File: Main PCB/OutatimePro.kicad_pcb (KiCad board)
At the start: 2 copper layers, 25.7 x 27.7 mm, 47 parts, among them IC1 PAM8904JPR, J1 USB_B_Micro_PCB_Edge_receptac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, J2 FH35C-9S-0.3SHW, J3 OSO_SWD, Q1 ALS-PT19-315C/L177/TR8, SW1 EVPAWED40, U1 ATSAML22N18A-CFUT, U2 MIC5365-3.3YMT, U3 USBLC6-2P6, U4 MAX40200ANS, Y1 32.768kHz

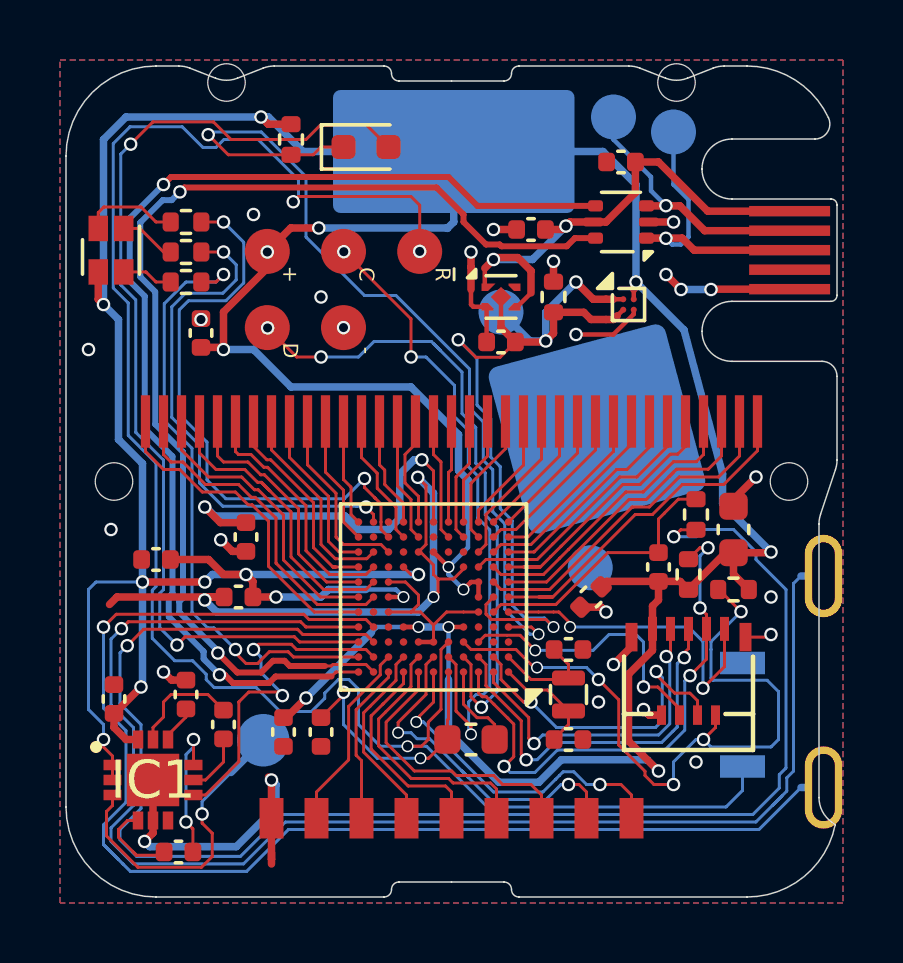
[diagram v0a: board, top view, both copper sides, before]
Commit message: move test pads to a good location
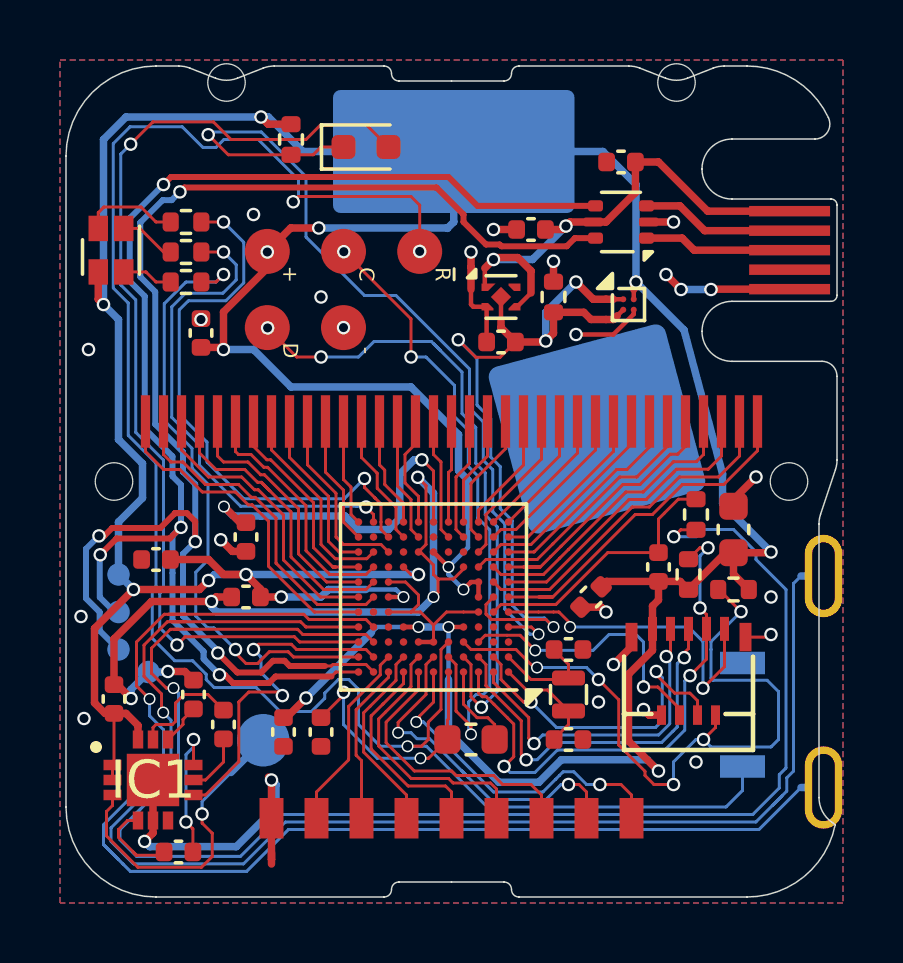
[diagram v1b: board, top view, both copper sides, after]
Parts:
- TP1, TP2, TP3, TP4: footprint OutatimePro:TestPoint_Pad_D1.5mm -> OutatimePro:TestPoint_Pad_D0.75mm
- moved TP1 25.3 mm to (14.8, 32.8)
- moved TP2 23.3 mm to (14.8, 31.5)
- moved TP3 15.5 mm to (14.8, 30.2)
- moved TP4 15.1 mm to (15.8, 33.5)
- moved C16 0.25 mm to (17.2, 34.2)
- moved C5 0.25 mm to (19.0, 31.0)
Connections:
- TP1 pad 1: Net-(J1-D+) -> /USB_P
- TP2 pad 1: Net-(J1-D-) -> /USB_N
- TP3 pad 1: +3.3V -> VCC
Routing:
- net /USB_P: track 38.1 -> 47.3 mm, vias 2 -> 4
- net /USB_N: track 38.0 -> 43.4 mm, vias 2 -> 4
- net VCC: track 151.5 -> 146.6 mm, vias 21 -> 19
- net Net-(J1-D+): track 9.59 -> 4.94 mm, vias 1 -> 0
- net GND: track 59.3 -> 63.2 mm, vias 29 -> 31
- net Net-(J1-D-): track 8.79 -> 5.11 mm, vias 1 -> 0
- net +3.3V: track 29.2 -> 27.3 mm
- net /VLCD: track 13.2 -> 11.9 mm
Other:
- board text added: "D+"
- board text added: "D-"
- board text added: "G"
- board text added: "V"

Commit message: move test pads more and change version format
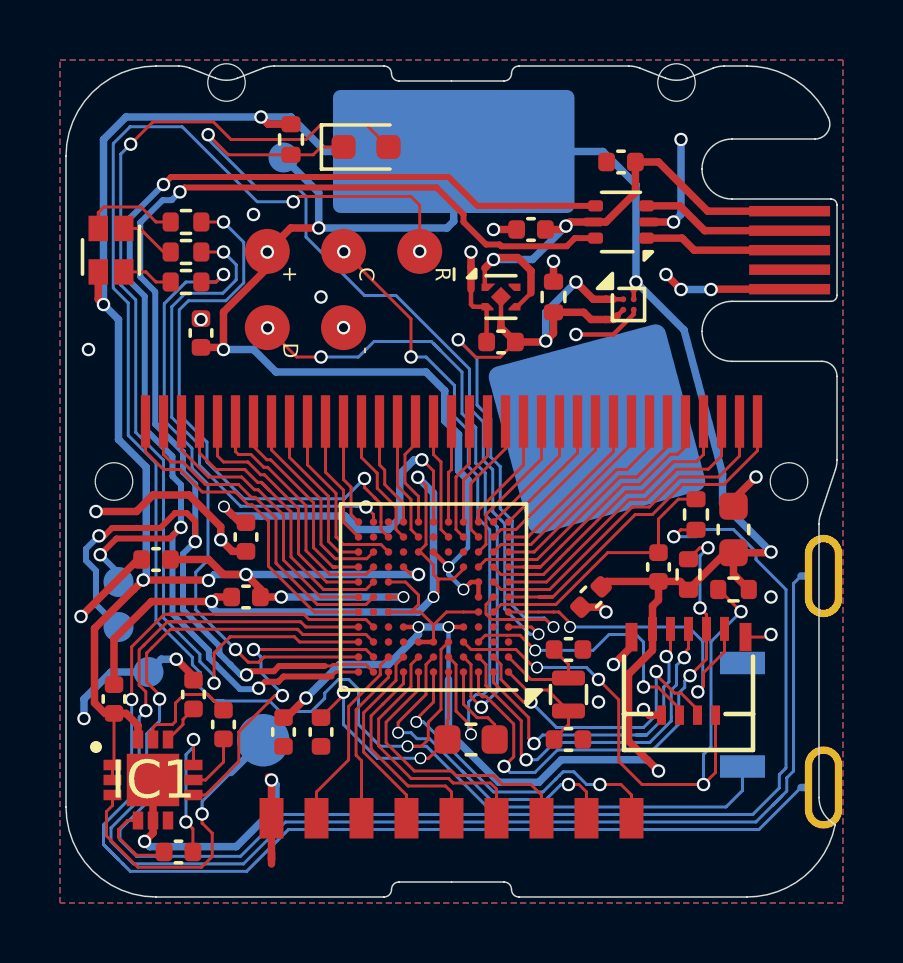
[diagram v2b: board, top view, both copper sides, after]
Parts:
- TP1, TP2, TP3, TP4: footprint OutatimePro:TestPoint_Pad_D0.75mm -> OutatimePro:TestPoint_Pad_D1.0mm
- moved TP3 14.9 mm to (20.2, 16.4)
- moved TP2 1.00 mm to (14.8, 30.5)
- moved TP1 0.75 mm to (14.8, 32.0)
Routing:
- net GND: track 63.2 -> 76.0 mm
- net VCC: track 146.6 -> 149.1 mm
- net /SCL: track 23.5 -> 21.0 mm, vias 5 -> 4
- net /~{LS_ENABLE}: track 33.6 -> 35.2 mm
- net /USB_N: track 43.4 -> 42.4 mm
- net /USB_P: track 47.3 -> 46.4 mm
- net /~{TS_ENABLE}: track 51.5 -> 50.7 mm
- net /BUZZER: track 12.8 -> 12.0 mm
- net /~{RESET}: track 60.4 -> 59.6 mm
- net /BTN_ADJUST: track 43.2 -> 42.5 mm
- net /A1_SCK: track 11.2 -> 10.6 mm
- net /BTN_MODE: track 48.2 -> 47.7 mm
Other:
- board text added: "v260827"
- board text removed: "V"
- board text removed: "v270826"

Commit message: resolve some drc errors, add cap to rgb led
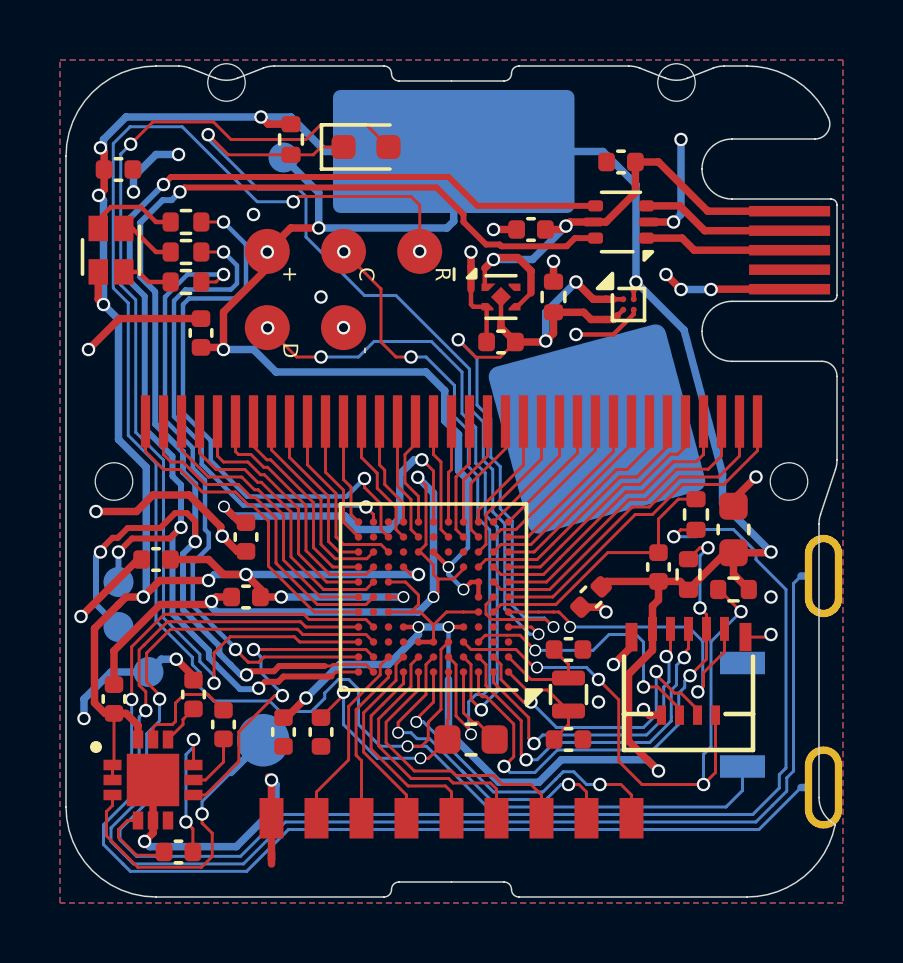
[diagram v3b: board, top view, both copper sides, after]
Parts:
- added C18: 0.1uF, Capacitor_SMD:C_0402_1005Metric, F.Cu at (14.8, 16.8)
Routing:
- net GND: track 76.0 -> 82.1 mm, vias 31 -> 32
- net /BTN_ADJUST: track 42.5 -> 41.2 mm
- net /BTN_MODE: track 47.7 -> 46.7 mm
- net /USB_N: track 42.4 -> 41.6 mm
- net VCC: track 149.1 -> 150.0 mm, vias 19 -> 21
- net /A2_MOSI: track 13.4 -> 12.8 mm
- net /SEG27: track 8.96 -> 8.40 mm

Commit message: make text consistent with programming header near test pad
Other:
- board text added: "-"
- board text removed: "G"
